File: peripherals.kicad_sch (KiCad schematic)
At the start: 26 parts, among them J2 Micro_SD_Card_Det_Hirose_DM3AT, J3 705510001, J4 705510001, U10 MAX98357A, U8 JLX256128G-931-PL_SPI, U9 USBLC6-2SC6

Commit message: Initial layout before routing.
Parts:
- removed C19, C20, C21, C22: 10u, Capacitor_SMD:C_0603_1608Metric_Pad1.08x0.95mm_HandSolder, symbol Device:C_Small
- removed R15: 330k, Resistor_SMD:R_0603_1608Metric_Pad0.98x0.95mm_HandSolder, symbol Device:R_Small
- added R20: 330k, Resistor_SMD:R_0603_1608Metric_Pad0.98x0.95mm_HandSolder, symbol Device:R_Small
- renumbered C18 to C17, C17 to C18, C23 to C19, C24 to C20, C25 to C21, C26 to C22, R16 to R19, R17 to R21, R18 to R22, R19 to R23, R20 to R24, R21 to R25, R22 to R26, R23 to R27, U9 to U10, U10 to U11, U8 to U9
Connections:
- net +3.3V_LCD is gone; now on net +3.3V_MCU: C16.1, C18.1, U9.[7,11-14,19,20] (VDD)
- net +3.3V_PERIPH: now also R20.2
- net SD_DET: now also J2.10 (DET_A); no longer J2.9 (DET_B)
- net at U11.10 (OUTN): now also J4.1 (Pin_1); no longer J4.2 (Pin_2)
- net at U11.9 (OUTP): now also J4.2 (Pin_2); no longer J4.1 (Pin_1)
- new net: J2.9 (DET_B), R20.1
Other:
- moved on the sheet: C17, R19

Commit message: PCB layout done, signal routing finished, power routing remaining.
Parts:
- renumbered R19 to R20, R20 to R21, R21 to R22, R22 to R23, R23 to R24, R24 to R25, R25 to R26, R26 to R27, R27 to R28
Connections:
- net ACOM_OD: now also U10.3 (I/O2); no longer U10.1 (I/O1)
- net at U10.4 (I/O2): now also J3.1 (Pin_1)
- net at U10.6 (I/O1): no longer J3.1 (Pin_1)
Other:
- moved on the sheet: U10

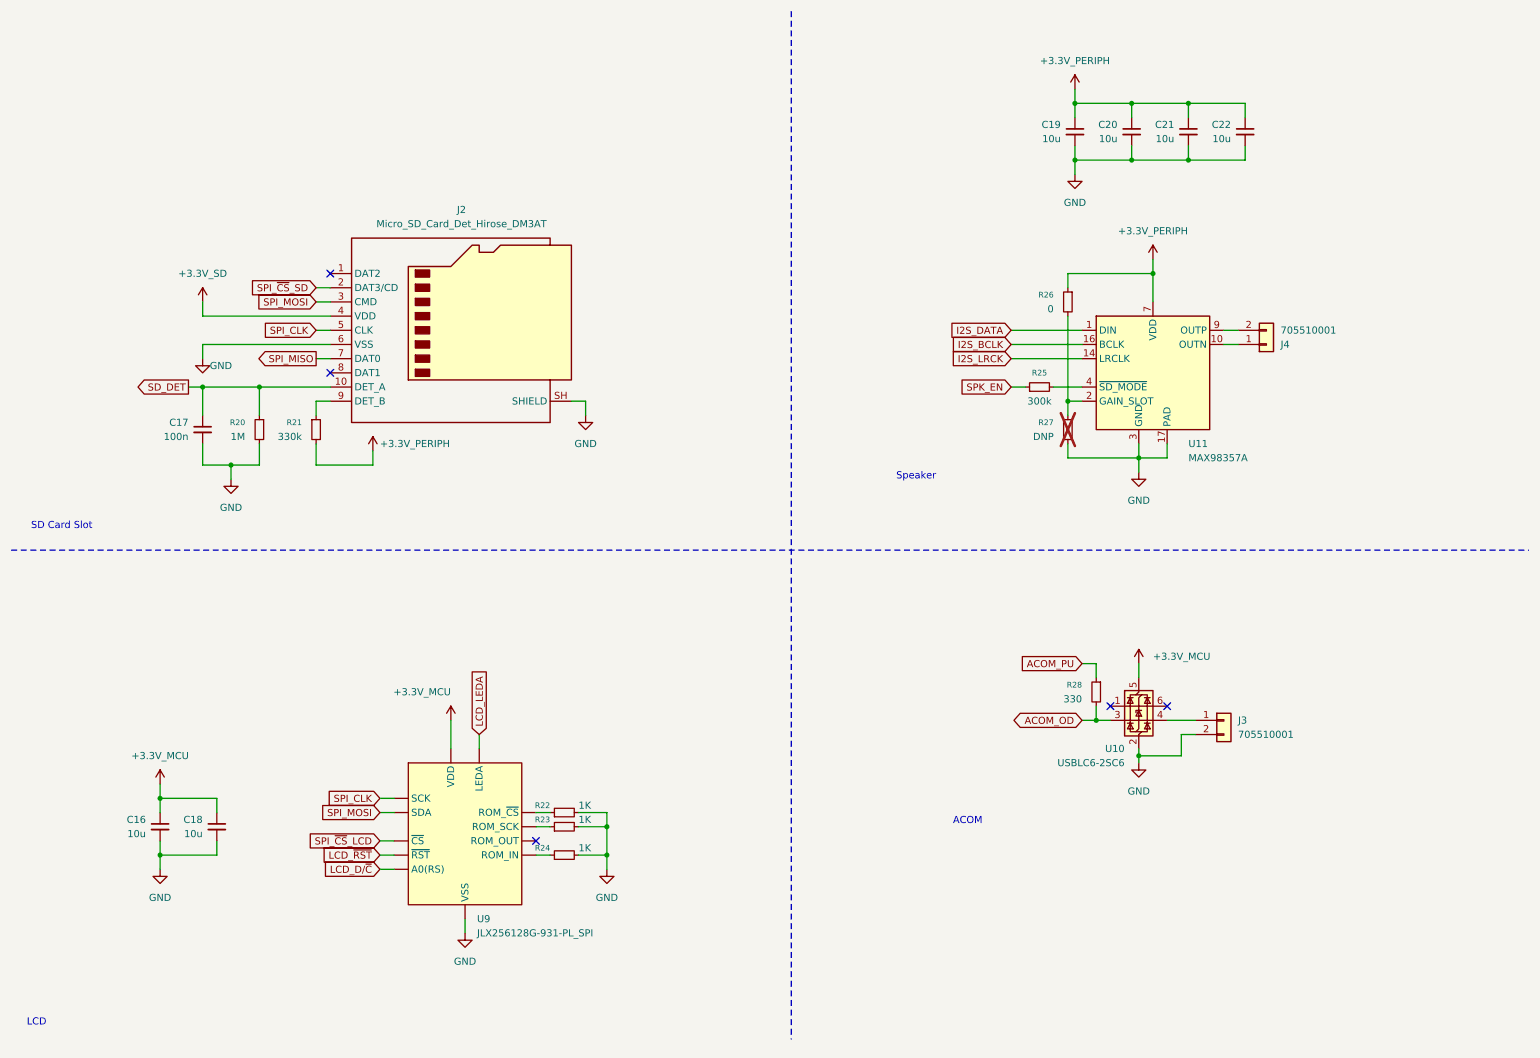
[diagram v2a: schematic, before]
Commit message: Revision to fix problems from first board fab
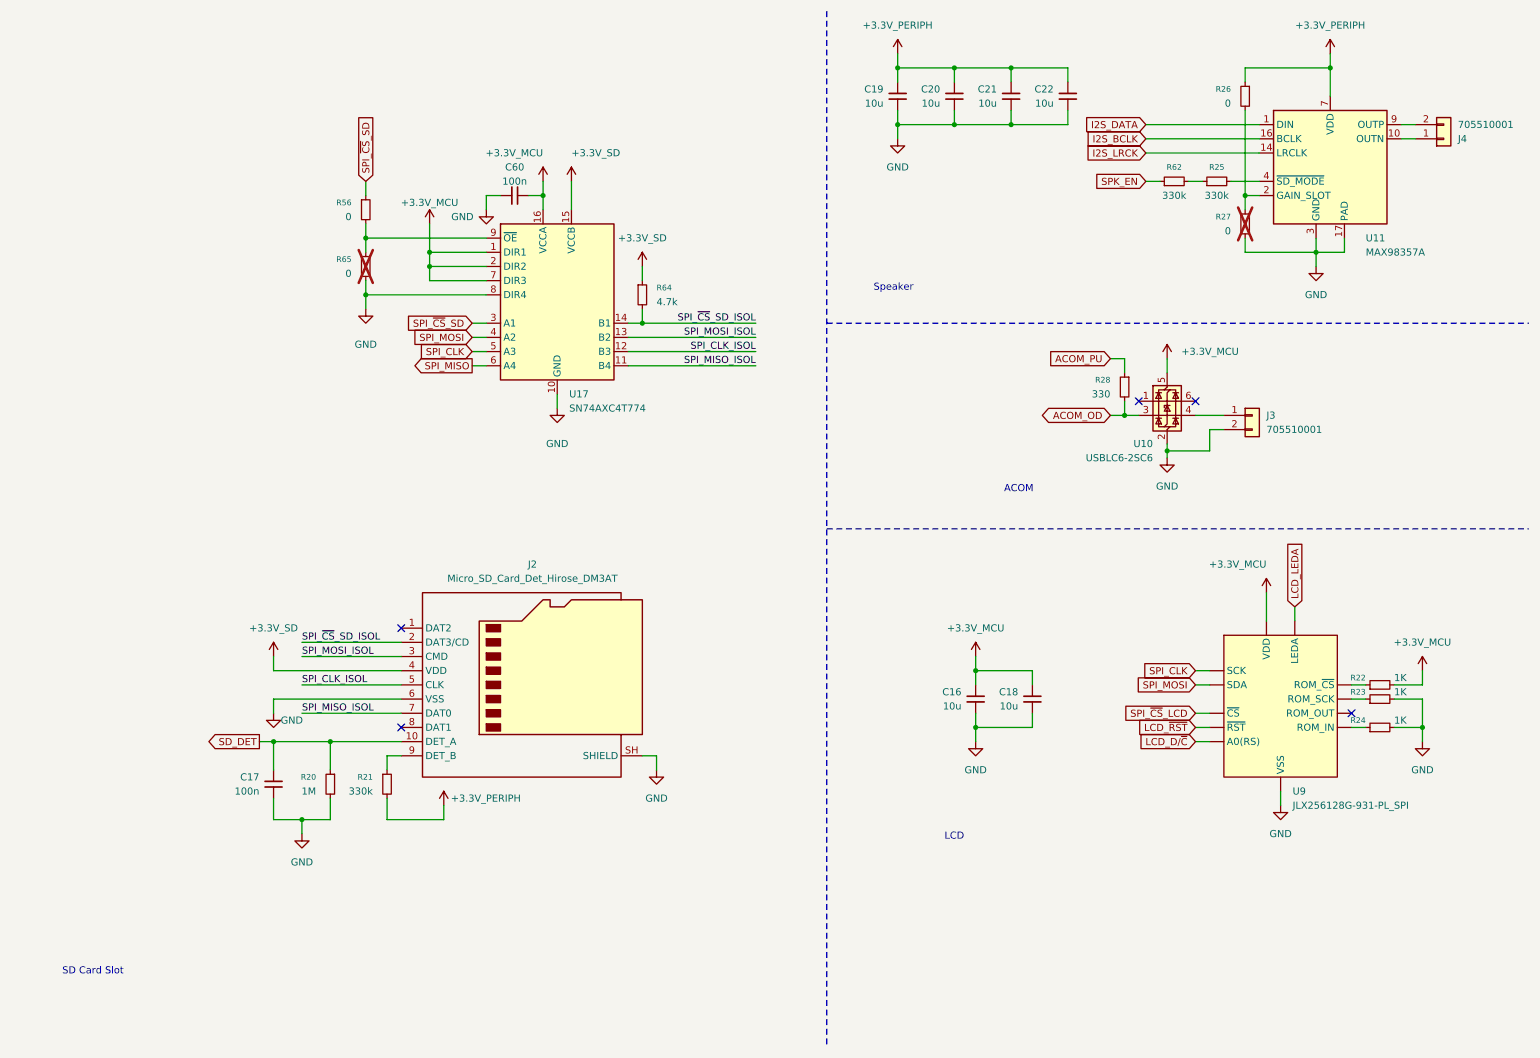
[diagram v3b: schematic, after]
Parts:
- added C60: 100n, Capacitor_SMD:C_0603_1608Metric_Pad1.08x0.95mm_HandSolder, symbol Device:C_Small
- added R56, R65: 0, Resistor_SMD:R_0603_1608Metric_Pad0.98x0.95mm_HandSolder, symbol Device:R_Small
- added R62: 330k, Resistor_SMD:R_0603_1608Metric_Pad0.98x0.95mm_HandSolder, symbol Device:R_Small
- added R64: 4.7k, Resistor_SMD:R_0603_1608Metric_Pad0.98x0.95mm_HandSolder, symbol Device:R_Small
- added U17: SN74AXC4T774, Package_SO:TSSOP-16_4.4x5mm_P0.65mm, symbol project_symbols:SN74AXC4T774
- R25: value 300k -> 330k
- R27: value DNP -> 0
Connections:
- net +3.3V_MCU: now also R22.2, C60.2, U17.1 (DIR1), U17.16 (VCCA), U17.2 (DIR2), U17.7 (DIR3)
- net +3.3V_SD: now also R64.1, U17.15 (VCCB)
- net GND: now also C60.1, R65.2, U17.10 (GND), U17.8 (DIR4); no longer R22.2
- net SPI_CLK: now also U17.5 (A3); no longer J2.5 (CLK)
- net SPI_MISO: now also U17.6 (A4); no longer J2.7 (DAT0)
- net SPI_MOSI: now also U17.4 (A2); no longer J2.3 (CMD)
- net SPI_~{CS}_SD: now also R56.1, U17.3 (A1); no longer J2.2 (DAT3/CD)
- net SPK_EN: now also R62.1; no longer R25.1
- new net: R56.2, R65.1, U17.9 (~{OE})
- new net: R25.1, R62.2
- new net SPI_CLK_ISOL: J2.5 (CLK), U17.12 (B3)
- new net SPI_MISO_ISOL: J2.7 (DAT0), U17.11 (B4)
- new net SPI_MOSI_ISOL: J2.3 (CMD), U17.13 (B2)
- new net SPI_~{CS}_SD_ISOL: J2.2 (DAT3/CD), R64.2, U17.14 (B1)
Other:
- moved on the sheet: C16, C17, C18, C19, C20, C21, C22, J2, J3, J4, R20, R21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

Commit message: Final version sent for fabrication
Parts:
- added R66: 1M, Resistor_SMD:R_0603_1608Metric_Pad0.98x0.95mm_HandSolder, symbol Device:R_Small
- R64: value 4.7k -> 3.3k
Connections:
- net +3.3V_MCU: now also R66.1
- net at R56.2, R65.1, U17.9 (~{OE}): now also R66.2
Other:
- moved on the sheet: R56, R65
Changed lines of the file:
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@@
 	)
 	(junction
+		(at 87.63 43.18)
+		(diameter 0)
+		(color 0 0 0 0)
+	)
+	(junction
 		(at 246.38 55.88)
 		(diameter 0)
@@
 	)
 	(junction
-		(at 76.2 53.34)
+		(at 72.39 53.34)
 		(diameter 0)
 		(color 0 0 0 0)
@@
 	)
 	(junction
-		(at 76.2 63.5)
+		(at 82.55 53.34)
+		(diameter 0)
+		(color 0 0 0 0)
+	)
+	(junction
+		(at 72.39 63.5)
 		(diameter 0)
 		(color 0 0 0 0)
@@
 	(wire
 		(pts
-			(xy 87.63 50.8) (xy 87.63 55.88)
+			(xy 87.63 40.64) (xy 87.63 43.18)
 		)
 		(stroke
@@
 	(wire
 		(pts
-			(xy 76.2 43.18) (xy 76.2 45.72)
+			(xy 72.39 43.18) (xy 72.39 45.72)
+		)
+		(stroke
+			(width 0)
+			(type default)
+		)
+	)
+	(wire
+		(pts
+			(xy 82.55 43.18) (xy 87.63 43.18)
 		)
 		(stroke
@@
 	(wire
 		(pts
+			(xy 87.63 43.18) (xy 87.63 55.88)
+		)
+		(stroke
+			(width 0)
+			(type default)
+		)
+	)
+	(wire
+		(pts
 			(xy 128.27 146.05) (xy 128.27 148.59)
 		)
@@
 	(wire
 		(pts
-			(xy 76.2 66.04) (xy 76.2 63.5)
+			(xy 72.39 66.04) (xy 72.39 63.5)
 		)
 		(stroke
@@
 	(wire
 		(pts
-			(xy 76.2 60.96) (xy 76.2 63.5)
+			(xy 72.39 60.96) (xy 72.39 63.5)
 		)
 		(stroke
@@
 	(wire
 		(pts
-			(xy 76.2 53.34) (xy 76.2 55.88)
+			(xy 72.39 53.34) (xy 72.39 55.88)
 		)
 		(stroke
@@
 	(wire
 		(pts
+			(xy 82.55 45.72) (xy 82.55 43.18)
+		)
+		(stroke
+			(width 0)
+			(type default)
+		)
+	)
+	(wire
+		(pts
 			(xy 82.55 138.43) (xy 64.77 138.43)
 		)
@@
 	(wire
 		(pts
+			(xy 82.55 53.34) (xy 97.79 53.34)
+		)
+		(stroke
+			(width 0)
+			(type default)
+		)
+	)
+	(wire
+		(pts
 			(xy 215.9 43.18) (xy 218.44 43.18)
 		)
@@
 	(wire
 		(pts
+			(xy 82.55 50.8) (xy 82.55 53.34)
+		)
+		(stroke
+			(width 0)
+			(type default)
+		)
+	)
+	(wire
+		(pts
 			(xy 224.79 138.43) (xy 227.33 138.43)
 		)
@@
 	(wire
 		(pts
-			(xy 76.2 50.8) (xy 76.2 53.34)
+			(xy 72.39 50.8) (xy 72.39 53.34)
 		)
 		(stroke
@@
 	(wire
 		(pts
-			(xy 76.2 53.34) (xy 97.79 53.34)
+			(xy 72.39 53.34) (xy 82.55 53.34)
 		)
 		(stroke
@@
 	(wire
 		(pts
-			(xy 76.2 63.5) (xy 97.79 63.5)
+			(xy 72.39 63.5) (xy 97.79 63.5)
 		)
 		(stroke
@@
 	(global_label "SPI_~{CS}_SD"
 		(shape input)
-		(at 76.2 43.18 90)
+		(at 72.39 43.18 90)
 		(fields_autoplaced yes)
 		(effects
@@
 		)
 		(property "Intersheetrefs" "${INTERSHEET_REFS}"
-			(at 76.2 30.2163 90)
+			(at 72.39 30.2163 90)
 			(hide yes)
 			(show_name no)
@@
 	(symbol
 		(lib_id "power:+3.3V")
-		(at 87.63 50.8 0)
+		(at 87.63 40.64 0)
 		(unit 1)
 		(body_style 1)
@@
 		(fields_autoplaced yes)
 		(property "Reference" "#PWR073"
-			(at 87.63 54.61 0)
+			(at 87.63 44.45 0)
 			(hide yes)
 			(show_name no)
@@
 		)
 		(property "Value" "+3.3V_MCU"
-			(at 87.63 46.99 0)
+			(at 87.63 36.83 0)
 			(show_name no)
 			(do_not_autoplace no)
@@
 		)
 		(property "Footprint" ""
-			(at 87.63 50.8 0)
+			(at 87.63 40.64 0)
 			(hide yes)
 			(show_name no)
@@
 		)
 		(property "Datasheet" ""
-			(at 87.63 50.8 0)
+			(at 87.63 40.64 0)
 			(hide yes)
 			(show_name no)
@@
 		)
 		(property "Description" "Power symbol creates a global label with name \"+3.3V\""
-			(at 87.63 50.8 0)
+			(at 87.63 40.64 0)
 			(hide yes)
 			(show_name no)
@@
 	(symbol
 		(lib_id "Device:R_Small")
-		(at 76.2 58.42 0)
+		(at 82.55 48.26 0)
+		(unit 1)
+		(body_style 1)
+		(exclude_from_sim no)
+		(in_bom yes)
+		(on_board yes)
+		(in_pos_files yes)
+		(dnp no)
+		(property "Reference" "R66"
+			(at 80.01 46.9899 0)
+			(show_name no)
+			(do_not_autoplace no)
+			(effects
+				(font
+					(size 1.016 1.016)
+				)
+				(justify right)
+			)
+		)
+		(property "Value" "1M"
+			(at 80.01 49.5299 0)
+			(show_name no)
+			(do_not_autoplace no)
+			(effects
+				(font
+					(size 1.27 1.27)
+				)
+				(justify right)
+			)
+		)
+		(property "Footprint" "Resistor_SMD:R_0603_1608Metric_Pad0.98x0.95mm_HandSolder"
+			(at 82.55 48.26 0)
+			(hide yes)
+			(show_name no)
+			(do_not_autoplace no)
+			(effects
+				(font
+					(size 1.27 1.27)
+				)
+			)
+		)
+		(property "Datasheet" ""
+			(at 82.55 48.26 0)
+			(hide yes)
+			(show_name no)
+			(do_not_autoplace no)
+			(effects
+				(font
+					(size 1.27 1.27)
+				)
+			)
+		)
+		(property "Description" "Resistor, small symbol"
+			(at 82.55 48.26 0)
+			(hide yes)
+			(show_name no)
+			(do_not_autoplace no)
+			(effects
+				(font
+					(size 1.27 1.27)
+				)
+			)
+		)
+		(pin "2"
+		)
+		(pin "1"
+		)
+		(instances
+			(project "DigiFur-Rev1.0"
+				(path "/71c692e8-0ff5-4766-b9b9-2b60ec4c8898"
+					(reference "R66")
+					(unit 1)
+				)
+			)
+		)
+	)
+	(symbol
+		(lib_id "Device:R_Small")
+		(at 72.39 58.42 0)
 		(unit 1)
 		(body_style 1)
@@
 		(dnp yes)
 		(property "Reference" "R65"
-			(at 73.66 57.1499 0)
+			(at 69.85 57.1499 0)
 			(show_name no)
 			(do_not_autoplace no)
@@
 		)
 		(property "Value" "0"
-			(at 73.66 59.6899 0)
+			(at 69.85 59.6899 0)
 			(show_name no)
 			(do_not_autoplace no)
@@
 		)
 		(property "Footprint" "Resistor_SMD:R_0603_1608Metric_Pad0.98x0.95mm_HandSolder"
-			(at 76.2 58.42 0)
+			(at 72.39 58.42 0)
 			(hide yes)
 			(show_name no)
@@
 		)
 		(property "Datasheet" ""
-			(at 76.2 58.42 0)
+			(at 72.39 58.42 0)
 			(hide yes)
 			(show_name no)
@@
 		)
 		(property "Description" "Resistor, small symbol"
-			(at 76.2 58.42 0)
+			(at 72.39 58.42 0)
 			(hide yes)
 			(show_name no)
@@
 	(symbol
 		(lib_id "Device:R_Small")
-		(at 76.2 48.26 0)
+		(at 72.39 48.26 0)
 		(unit 1)
 		(body_style 1)
@@
 		(dnp no)
 		(property "Reference" "R56"
-			(at 73.66 46.9899 0)
+			(at 69.85 46.9899 0)
 			(show_name no)
 			(do_not_autoplace no)
@@
 		)
 		(property "Value" "0"
-			(at 73.66 49.5299 0)
+			(at 69.85 49.5299 0)
 			(show_name no)
 			(do_not_autoplace no)
@@
 		)
 		(property "Footprint" "Resistor_SMD:R_0603_1608Metric_Pad0.98x0.95mm_HandSolder"
-			(at 76.2 48.26 0)
+			(at 72.39 48.26 0)
 			(hide yes)
 			(show_name no)
@@
 		)
 		(property "Datasheet" ""
-			(at 76.2 48.26 0)
+			(at 72.39 48.26 0)
 			(hide yes)
 			(show_name no)
@@
 		)
 		(property "Description" "Resistor, small symbol"
-			(at 76.2 48.26 0)
+			(at 72.39 48.26 0)
 			(hide yes)
 			(show_name no)
@@
 			)
 		)
-		(property "Value" "4.7k"
+		(property "Value" "3.3k"
 			(at 128.27 64.7699 0)
 			(show_name no)
@@
 	(symbol
 		(lib_id "power:GND")
-		(at 76.2 66.04 0)
+		(at 72.39 66.04 0)
 		(unit 1)
 		(body_style 1)
@@
 		(fields_autoplaced yes)
 		(property "Reference" "#PWR074"
-			(at 76.2 72.39 0)
+			(at 72.39 72.39 0)
 			(hide yes)
 			(show_name no)
@@
 		)
 		(property "Value" "GND"
-			(at 76.2 72.39 0)
+			(at 72.39 72.39 0)
 			(show_name no)
 			(do_not_autoplace no)
@@
 		)
 		(property "Footprint" ""
-			(at 76.2 66.04 0)
+			(at 72.39 66.04 0)
 			(hide yes)
 			(show_name no)
@@
 		)
 		(property "Datasheet" ""
-			(at 76.2 66.04 0)
+			(at 72.39 66.04 0)
 			(hide yes)
 			(show_name no)
@@
 		)
 		(property "Description" "Power symbol creates a global label with name \"GND\" , ground"
-			(at 76.2 66.04 0)
+			(at 72.39 66.04 0)
 			(hide yes)
 			(show_name no)
